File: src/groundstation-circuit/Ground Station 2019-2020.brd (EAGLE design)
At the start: 160 x 100 mm, 9 parts, among them U1 ADAFRUIT_RFM95W_LORA_RADIO

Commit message: Schematic and first routing attempt completed.
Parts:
- removed D1, D2, D3: (no value), SparkFun-LED:LED_5MM
- removed J1: (no value), SparkFun-Connectors:1X06
- added HC-05: (no value), SparkFun-Connectors:1X06
- added LED1, LED2, LED3: (no value), SparkFun-LED:LED_5MM
- added R4: 220, SparkFun-Resistors:AXIAL-0.3
- added R5: 1000, SparkFun-Resistors:AXIAL-0.3
- moved R3 180.9 mm to (120.7, 22.9), turned to 90 degrees
- moved R2 178.3 mm to (128.3, 22.9), turned to 90 degrees
- moved R1 175.8 mm to (135.9, 22.9), turned to 90 degrees
- moved U1 151.1 mm to (83.8, 11.4), turned to 90 degrees
- moved U$1 135.6 mm to (101.6, 49.5), turned to 90 degrees
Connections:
- new net CS: U$1.10, U1.8
- new net G0: U$1.8, U1.4
- new net LED1: R3.P$2, U$1.2
- new net LED2: R2.P$2, U$1.3
- new net LED3: R1.P$2, U$1.4
- new net MISO: U$1.12, U1.6
- new net MOSI: U$1.11, U1.7
- new net N$1: LED3.A, R1.P$1
- new net N$3: LED1.A, R3.P$1
- new net N$4: R4.P$2, U$1.1
- new net RST: U$1.9, U1.9
- new net RX1: HC-05.4, U$1.0
- new net SCK: U$1.13, U1.5
- new net TX1: HC-05.5, R4.P$1, R5.P$2
- net 3.3V: now also HC-05.2, U1.1
- net GND: now also HC-05.3, LED1.K, LED2.K, LED3.K, R5.P$1
- net N$2: now also LED2.A, R2.P$1; no longer U1.1
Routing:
- net 3.3V: track 0.00 -> 105.8 mm, vias 0 -> 1
- net RX1: track 0.00 -> 74.3 mm
- net TX1: track 0.00 -> 49.0 mm
- net LED3: track 0.00 -> 44.4 mm
- net SCK: track 0.00 -> 39.9 mm
- net N$4: track 0.00 -> 39.8 mm
- net LED2: track 0.00 -> 39.3 mm
- net LED1: track 0.00 -> 37.2 mm
- net G0: track 0.00 -> 21.6 mm
- net MISO: track 0.00 -> 20.0 mm
- net MOSI: track 0.00 -> 16.4 mm
- net CS: track 0.00 -> 12.1 mm
- net RST: track 0.00 -> 7.87 mm
- net N$3: track 0.00 -> 3.81 mm
- net N$2: track 0.00 -> 3.81 mm
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- added copper zone on layer 1, net GND
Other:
- board size 160 x 100 mm -> 57.1 x 69.5 mm

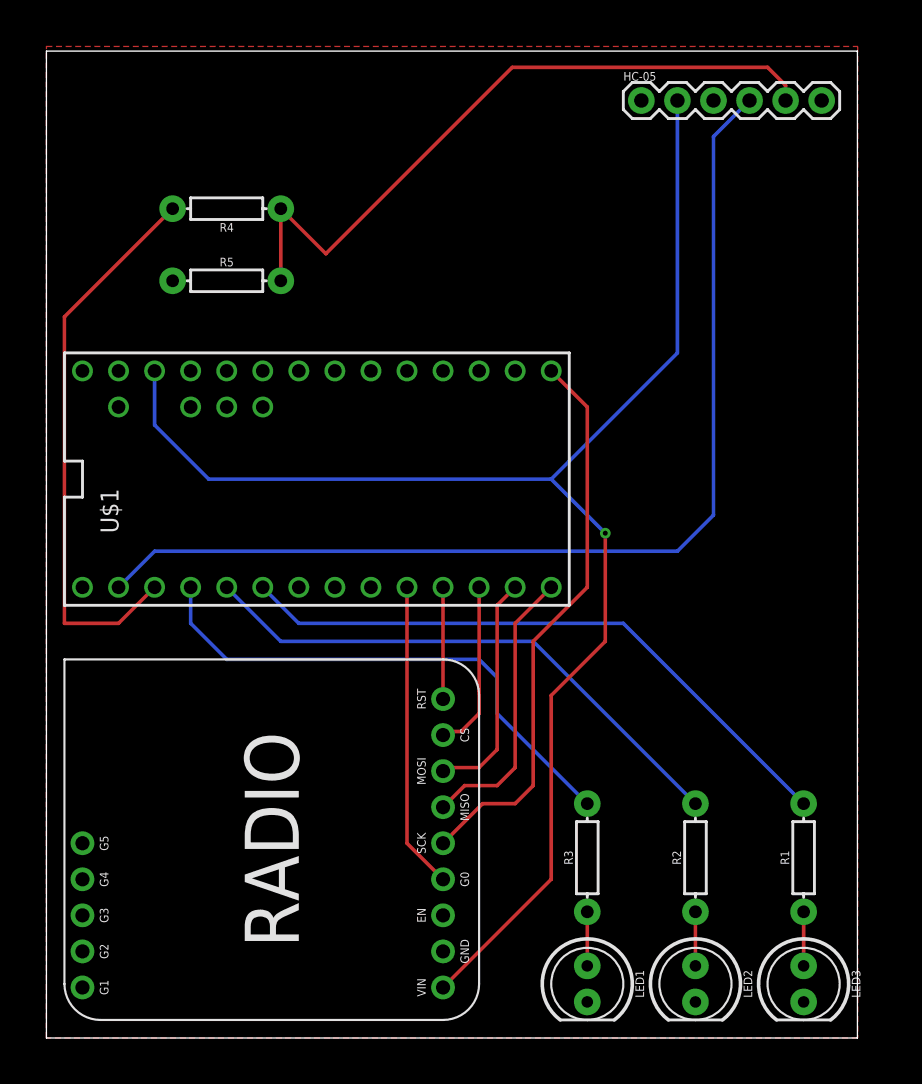
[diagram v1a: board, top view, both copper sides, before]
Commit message: Rounded board corners
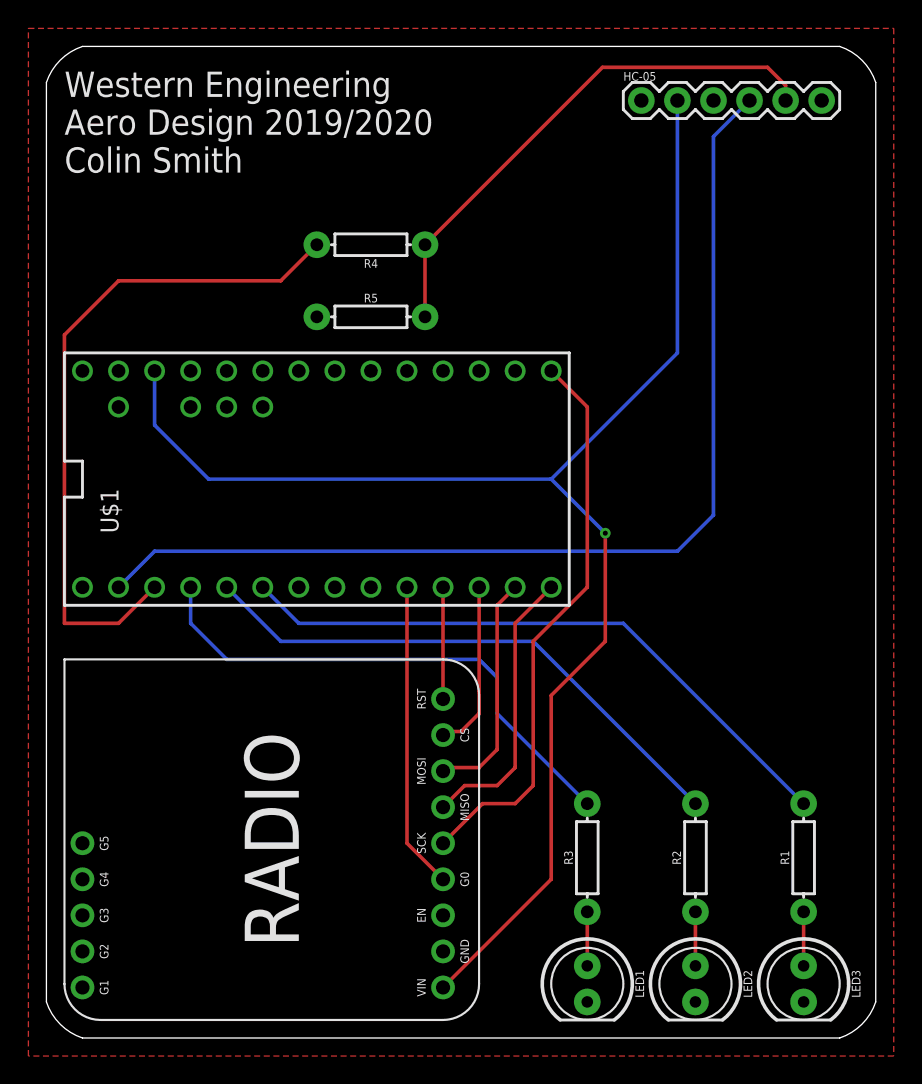
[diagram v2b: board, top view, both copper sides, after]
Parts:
- moved R5 10.5 mm to (105.4, 61.0)
- moved R4 10.5 mm to (105.4, 66.0)
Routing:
- net TX1: track 49.0 -> 37.2 mm
- net N$4: track 39.8 -> 48.1 mm
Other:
- board size 57.1 x 69.5 mm -> 58.4 x 69.9 mm
- board text added: "Western Engineering Aero Design 2019/2020 Colin Smith"
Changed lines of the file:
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@@
 <board>
 <plain>
-<wire x1="82.55" y1="10.16" x2="139.68" y2="10.16" width="0" layer="20"/>
-<wire x1="139.68" y1="10.16" x2="139.68" y2="79.68" width="0" layer="20"/>
-<wire x1="139.68" y1="79.68" x2="82.55" y2="79.68" width="0" layer="20"/>
-<wire x1="82.55" y1="79.68" x2="82.55" y2="10.16" width="0" layer="20"/>
+<text x="83.82" y="71.12" size="1.778" layer="21">Western Engineering
+Aero Design 2019/2020
+Colin Smith</text>
+<wire x1="85.09" y1="10.16" x2="138.43" y2="10.16" width="0" layer="20"/>
+<wire x1="82.55" y1="77.47" x2="82.55" y2="12.7" width="0" layer="20"/>
+<wire x1="85.09" y1="80.01" x2="138.43" y2="80.01" width="0" layer="20"/>
+<wire x1="140.97" y1="77.47" x2="140.97" y2="12.7" width="0" layer="20"/>
+<wire x1="82.55" y1="77.47" x2="85.09" y2="80.01" width="0" layer="20" curve="-53.130102"/>
+<wire x1="138.43" y1="80.01" x2="140.97" y2="77.47" width="0" layer="20" curve="-53.130102"/>
+<wire x1="85.09" y1="10.16" x2="82.55" y2="12.7" width="0" layer="20" curve="-53.130102"/>
+<wire x1="140.97" y1="12.7" x2="138.43" y2="10.16" width="0" layer="20" curve="-53.130102"/>
 </plain>
 <attributes>
@@
 <element name="U$1" library="Teensy_3_and_LC_Series_Boards_v1.4" package="TEENSY_3.0-3.2&amp;LC_DIL+4" value="TEENSY_3.1-3.2_DIL+4" x="101.6" y="49.53" rot="R90"/>
 <element name="U1" library="AERO_Eagle_Library" package="ADAFRUIT_RFM95W_LORA_RADIO" value="ADAFRUIT_RFM95W_LORA_RADIO" x="83.82" y="11.43" rot="R90"/>
-<element name="R4" library="SparkFun-Resistors" library_urn="urn:adsk.eagle:library:532" package="AXIAL-0.3" package3d_urn="urn:adsk.eagle:package:39658/1" value="220" x="95.25" y="68.58" rot="R180">
-<attribute name="PROD_ID" value="RES-8371" x="95.25" y="68.58" size="1.778" layer="27" rot="R180" display="off"/>
-</element>
-<element name="R5" library="SparkFun-Resistors" library_urn="urn:adsk.eagle:library:532" package="AXIAL-0.3" package3d_urn="urn:adsk.eagle:package:39658/1" value="1000" x="95.25" y="63.5">
-<attribute name="PROD_ID" value="RES-8371" x="95.25" y="63.5" size="1.778" layer="27" display="off"/>
+<element name="R4" library="SparkFun-Resistors" library_urn="urn:adsk.eagle:library:532" package="AXIAL-0.3" package3d_urn="urn:adsk.eagle:package:39658/1" value="220" x="105.41" y="66.04" rot="R180">
+<attribute name="PROD_ID" value="RES-8371" x="105.41" y="66.04" size="1.778" layer="27" rot="R180" display="off"/>
+</element>
+<element name="R5" library="SparkFun-Resistors" library_urn="urn:adsk.eagle:library:532" package="AXIAL-0.3" package3d_urn="urn:adsk.eagle:package:39658/1" value="1000" x="105.41" y="60.96">
+<attribute name="PROD_ID" value="RES-8371" x="105.41" y="60.96" size="1.778" layer="27" display="off"/>
 </element>
 </elements>
@@
 <contactref element="HC-05" pad="3"/>
 <polygon width="0.1524" layer="1">
-<vertex x="82.55" y="80.01"/>
-<vertex x="139.7" y="80.01"/>
-<vertex x="139.7" y="10.16"/>
-<vertex x="82.55" y="10.16"/>
+<vertex x="81.28" y="81.28"/>
+<vertex x="142.24" y="81.28"/>
+<vertex x="142.24" y="8.89"/>
+<vertex x="81.28" y="8.89"/>
 </polygon>
 <contactref element="R5" pad="P$1"/>
@@
 <contactref element="R4" pad="P$1"/>
 <contactref element="R5" pad="P$2"/>
-<wire x1="99.06" y1="68.58" x2="102.235" y2="65.405" width="0.254" layer="1"/>
-<wire x1="99.06" y1="68.58" x2="99.06" y2="63.5" width="0.254" layer="1"/>
-<wire x1="102.235" y1="65.405" x2="115.367" y2="78.537" width="0.254" layer="1"/>
-<wire x1="115.367" y1="78.537" x2="133.35" y2="78.537" width="0.254" layer="1"/>
 <wire x1="133.35" y1="78.537" x2="134.62" y2="77.267" width="0.254" layer="1"/>
 <wire x1="134.62" y1="77.267" x2="134.62" y2="76.2" width="0.254" layer="1"/>
+<wire x1="109.22" y1="66.04" x2="109.22" y2="60.96" width="0.254" layer="1"/>
+<wire x1="109.22" y1="66.04" x2="121.717" y2="78.537" width="0.254" layer="1"/>
+<wire x1="121.717" y1="78.537" x2="133.35" y2="78.537" width="0.254" layer="1"/>
 </signal>
 <signal name="SCK">
@@
 <wire x1="90.17" y1="41.91" x2="87.63" y2="39.37" width="0.254" layer="1"/>
 <wire x1="87.63" y1="39.37" x2="83.82" y2="39.37" width="0.254" layer="1"/>
-<wire x1="83.82" y1="39.37" x2="83.82" y2="60.96" width="0.254" layer="1"/>
-<wire x1="83.82" y1="60.96" x2="91.44" y2="68.58" width="0.254" layer="1"/>
+<wire x1="83.82" y1="39.37" x2="83.82" y2="59.69" width="0.254" layer="1"/>
+<wire x1="83.82" y1="59.69" x2="87.63" y2="63.5" width="0.254" layer="1"/>
+<wire x1="87.63" y1="63.5" x2="99.06" y2="63.5" width="0.254" layer="1"/>
+<wire x1="99.06" y1="63.5" x2="101.6" y2="66.04" width="0.254" layer="1"/>
 </signal>
 </signals>
@@
 </drawing>
 <compatibility>
+<note version="6.3" minversion="6.2.2" severity="warning">
+Since Version 6.2.2 text objects can contain more than one line,
+which will not be processed correctly with this version.
+</note>
 <note version="8.2" severity="warning">
 Since Version 8.2, EAGLE supports online libraries. The ids

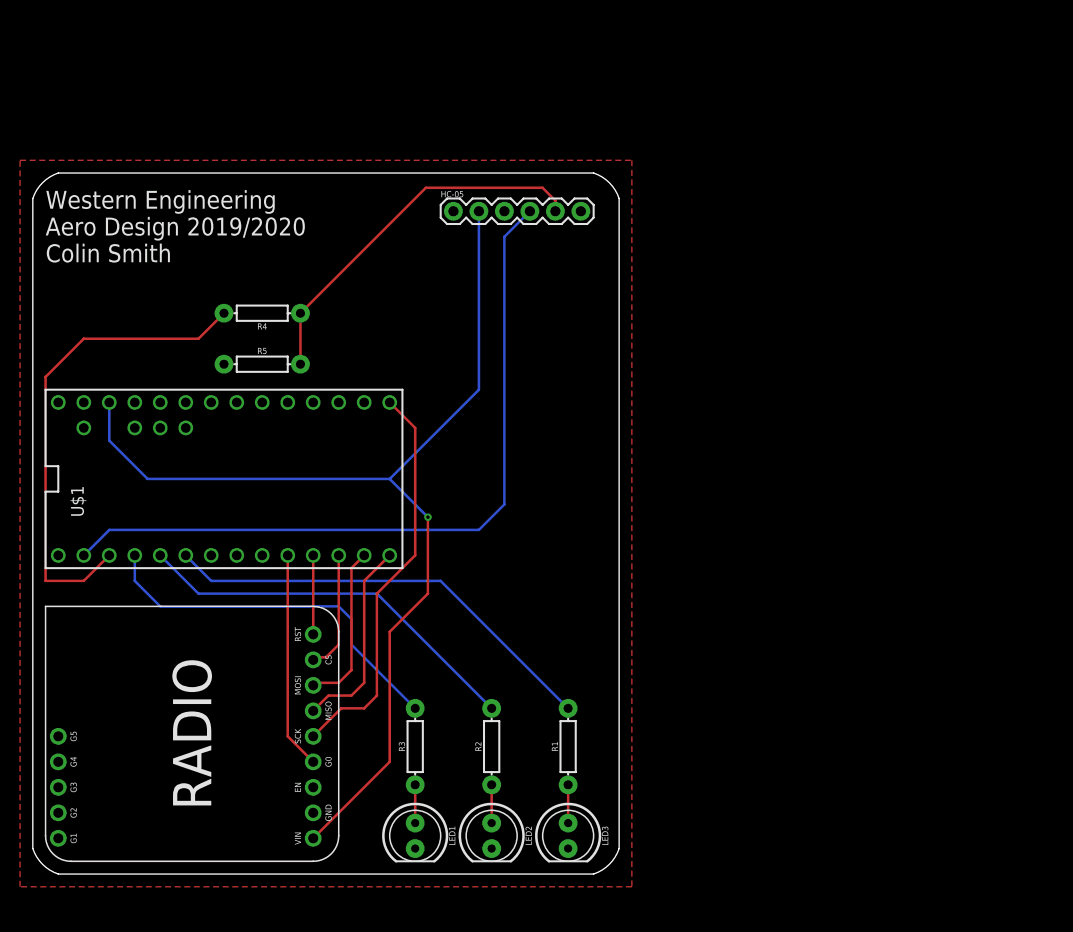
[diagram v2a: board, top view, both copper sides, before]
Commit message: Added LCD to board and increased space to accomidate
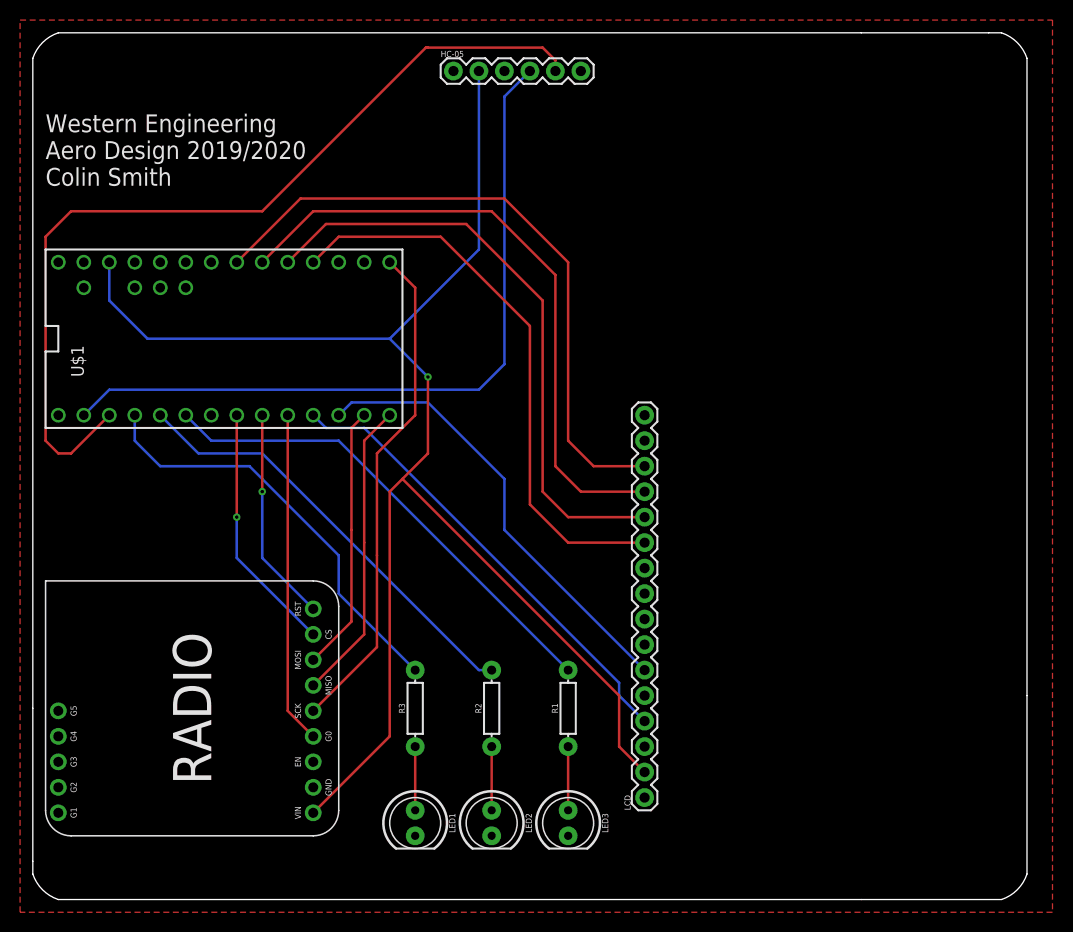
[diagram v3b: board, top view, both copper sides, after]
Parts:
- removed R4: 220, SparkFun-Resistors:AXIAL-0.3
- removed R5: 1000, SparkFun-Resistors:AXIAL-0.3
- added LCD: (no value), SparkFun-Connectors:1X16
- moved HC-05 14.0 mm to (124.5, 90.2)
- moved U$1 14.0 mm to (101.6, 63.5)
- moved R1 3.81 mm to (135.9, 26.7)
- moved R2 3.81 mm to (128.3, 26.7)
- moved R3 3.81 mm to (120.7, 26.7)
- moved U1 2.54 mm to (83.8, 14.0)
- moved LED1 1.27 mm to (120.7, 15.2)
- moved LED2 1.27 mm to (128.3, 15.2)
- moved LED3 1.27 mm to (135.9, 15.2)
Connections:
- removed net N$4: R4.P$2, U$1.1
- new net D4: LCD.11, U$1.16/A2
- new net D5: LCD.12, U$1.17/A3
- new net D6: LCD.13, U$1.18/A4
- new net D7: LCD.14, U$1.19/A5
- new net LCD_RX: LCD.4, U$1.9
- new net LCD_TX: LCD.6, U$1.10
- net 3.3V: now also LCD.2
- net CS: now also U$1.6; no longer U$1.10
- net GND: now also LCD.1, LCD.3, LCD.5; no longer R5.P$1
- net RST: now also U$1.7; no longer U$1.9
- net TX1: now also U$1.1; no longer R4.P$1, R5.P$2
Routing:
- net D7: track 0.00 -> 64.7 mm
- net D6: track 0.00 -> 62.9 mm
- net D5: track 0.00 -> 60.4 mm
- net D4: track 0.00 -> 57.1 mm
- net TX1: track 37.2 -> 89.0 mm
- net 3.3V: track 105.8 -> 156.4 mm
- net N$4: track 48.1 -> 0.00 mm
- net LCD_RX: track 0.00 -> 46.4 mm
- net LCD_TX: track 0.00 -> 45.0 mm
- net RST: track 7.87 -> 21.4 mm, vias 0 -> 1
- net CS: track 12.1 -> 25.0 mm, vias 0 -> 1
- net G0: track 21.6 -> 33.1 mm
- net MISO: track 20.0 -> 30.1 mm
- net MOSI: track 16.4 -> 26.5 mm
- net SCK: track 39.9 -> 50.0 mm
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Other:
- board size 58.4 x 69.9 mm -> 99.1 x 86.4 mm

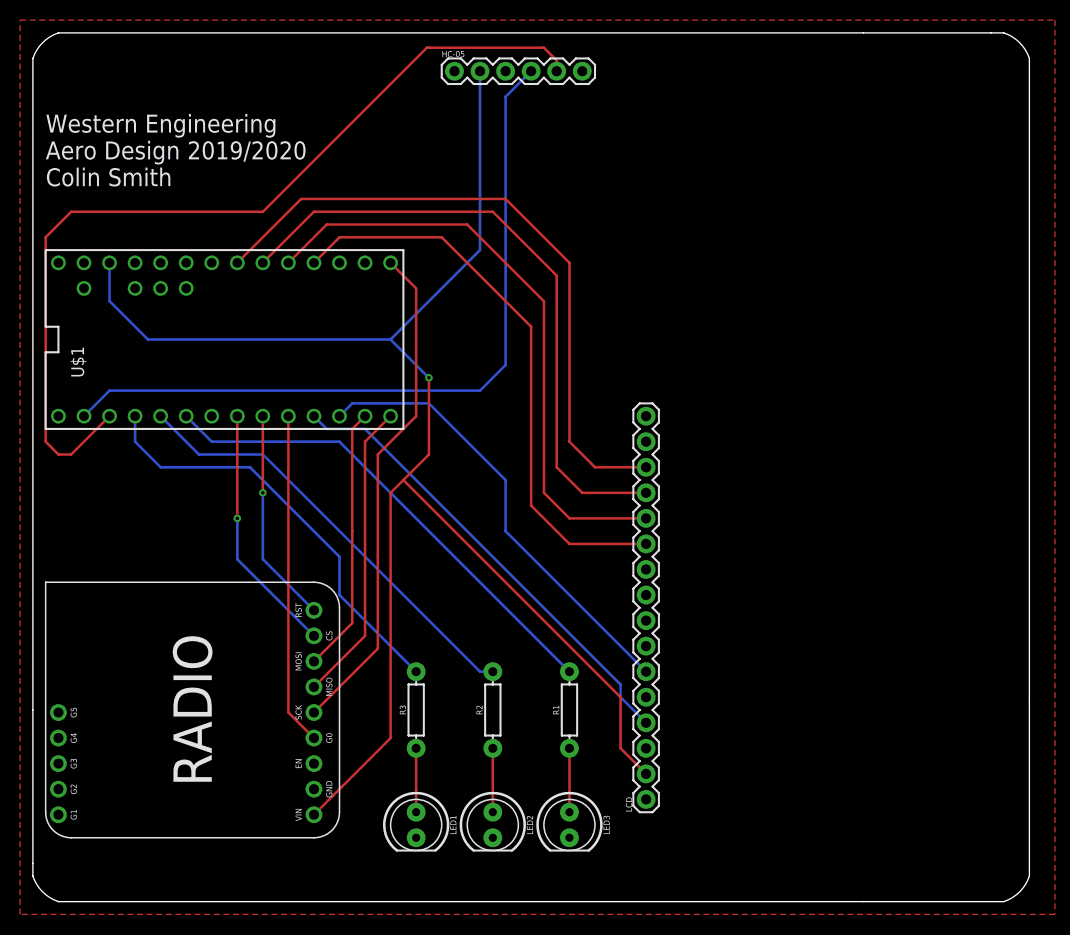
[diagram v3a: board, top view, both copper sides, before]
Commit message: Added additional LCD, mounting holes and slik screen.
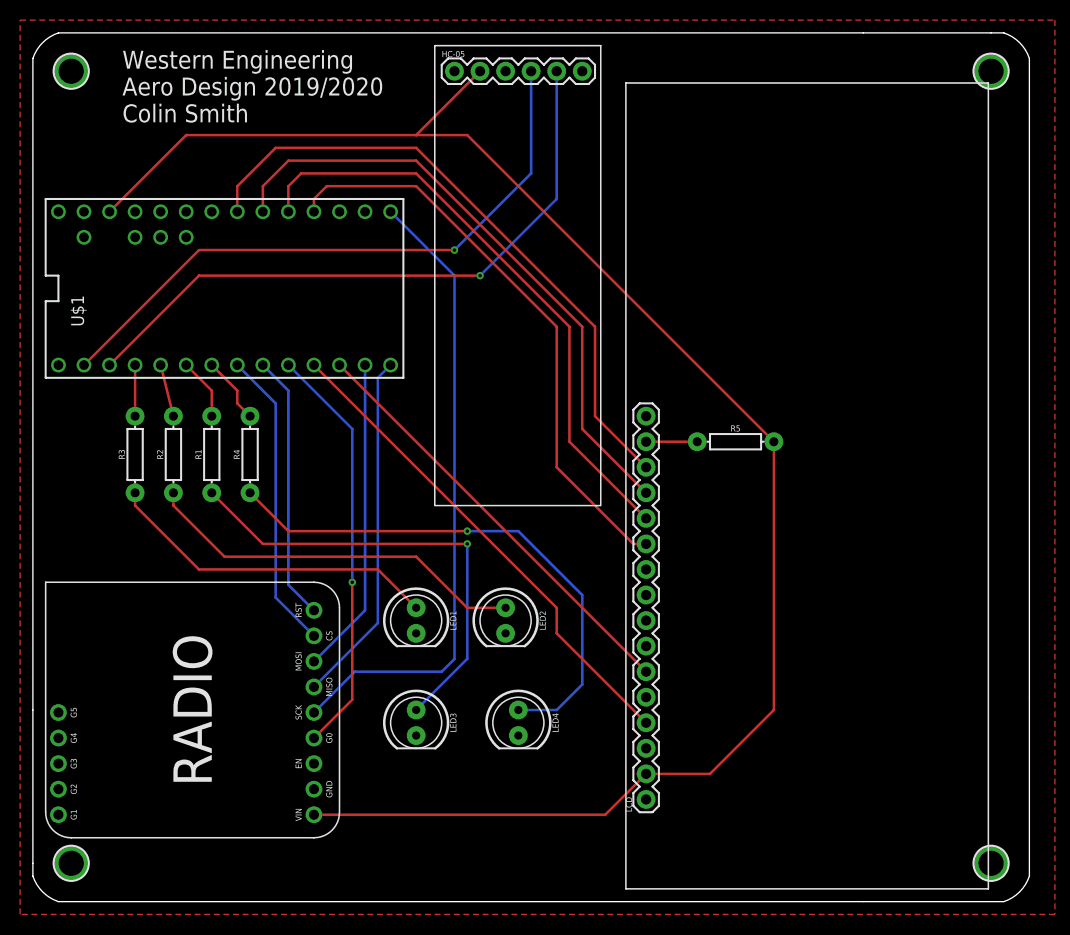
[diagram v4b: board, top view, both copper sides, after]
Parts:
- added LED4: (no value), SparkFun-LED:LED_5MM
- added R4: 330, SparkFun-Resistors:AXIAL-0.3
- added R5: 220, SparkFun-Resistors:AXIAL-0.3
- added U$2, U$3, U$4, U$5: MOUNTINGHOLE2.5, microbuilder:MOUNTINGHOLE_2.5_PLATED
- moved R1 43.7 mm to (100.3, 52.1)
- moved R2 40.7 mm to (96.5, 52.1)
- moved R3 37.8 mm to (92.7, 52.1)
- moved LED2 20.4 mm to (129.5, 35.6)
- moved LED1 20.3 mm to (120.7, 35.6)
- moved LED3 18.3 mm to (120.7, 25.4)
- moved U$1 5.08 mm to (101.6, 68.6)
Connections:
- new net LED4: R4.P$2, U$1.5
- new net N$4: LCD.15, R5.P$1
- new net N$5: LED4.A, R4.P$1
- net 3.3V: now also R5.P$2
- net GND: now also LCD.16, LED4.K
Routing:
- net N$5: track 0.00 -> 53.5 mm, vias 0 -> 1
- net LED3: track 48.6 -> 6.13 mm
- net N$1: track 6.35 -> 46.1 mm, vias 0 -> 1
- net LED2: track 43.5 -> 5.24 mm
- net LED1: track 42.2 -> 5.08 mm
- net N$2: track 6.35 -> 38.5 mm
- net N$3: track 6.35 -> 33.4 mm
- net TX1: track 89.0 -> 64.0 mm, vias 0 -> 1
- net SCK: track 50.0 -> 63.3 mm
- net RX1: track 74.3 -> 62.5 mm, vias 0 -> 1
- net 3.3V: track 156.4 -> 167.5 mm, vias 1 -> 0
- net G0: track 33.1 -> 41.3 mm, vias 0 -> 1
- net LED4: track 0.00 -> 6.66 mm
- net N$4: track 0.00 -> 5.08 mm
- net RST: track 21.4 -> 26.5 mm, vias 1 -> 0
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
